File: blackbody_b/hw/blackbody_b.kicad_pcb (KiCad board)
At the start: 4 copper layers, 90 x 60 mm, 53 parts, among them IC101 TSL25911FN, IC201 ADM3055EBRIZ, J101 43650-0227, J201 43650-0427, J202 43650-0427, U101 NUCLEO-L432KC

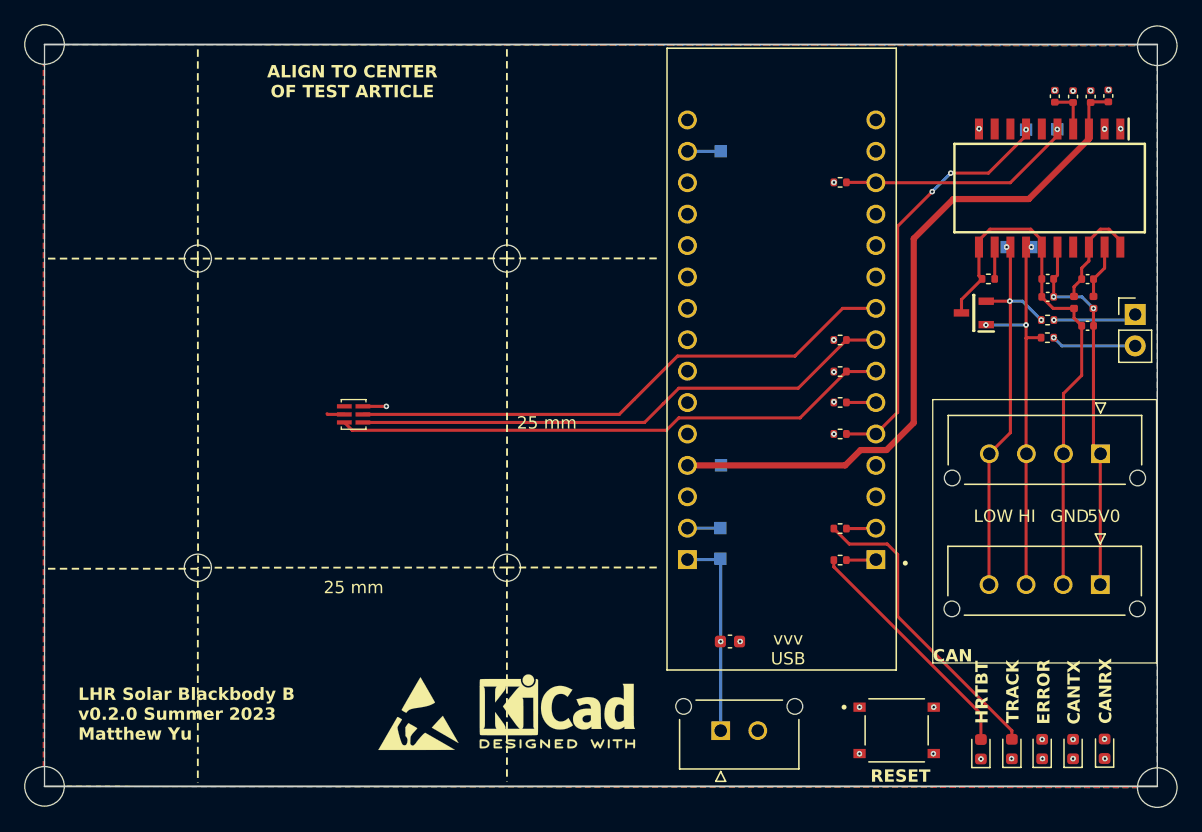
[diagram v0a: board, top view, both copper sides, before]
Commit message: fixes for blackbody b before prod
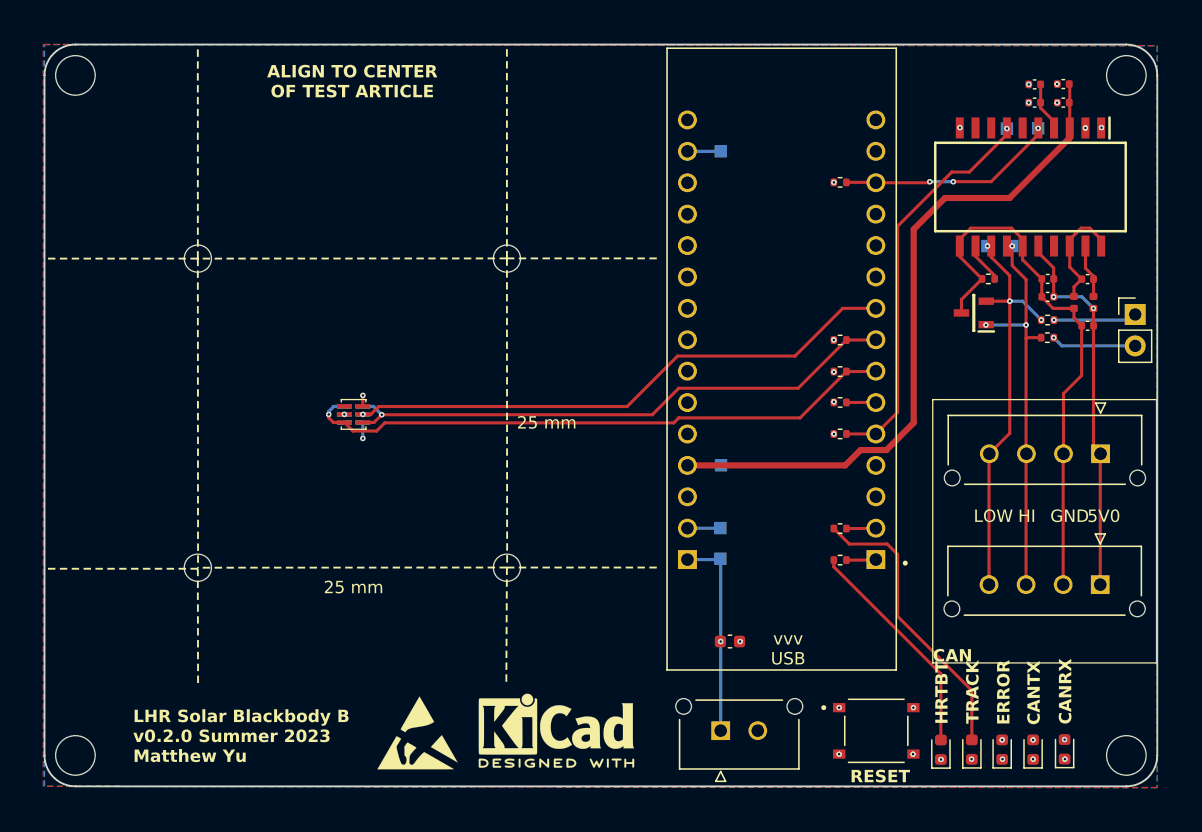
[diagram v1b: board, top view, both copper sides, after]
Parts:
- added IC102: TSL25911FN, footprints:ams_TSL25911FN, B.Cu at (115.0, 89.9)
- moved C201 3.76 mm to (172.4, 63.2), turned to 180 degrees
- moved H102 3.61 mm to (177.5, 117.5)
- moved H103 3.54 mm to (92.5, 62.5)
- moved H104 3.54 mm to (92.5, 117.5)
- moved H101 3.47 mm to (177.5, 62.5)
- moved D102 3.24 mm to (165.0, 117.0)
- moved D103 3.24 mm to (162.5, 117.0)
- moved D105 3.24 mm to (172.5, 117.0)
- moved D101 3.24 mm to (167.5, 117.0)
- moved D104 3.24 mm to (170.0, 117.0)
- moved C204 3.14 mm to (170.1, 64.7), turned to 180 degrees
- moved C202 2.27 mm to (172.4, 64.7), turned to 180 degrees
- moved C203 1.89 mm to (170.1, 63.2), turned to 180 degrees
- moved S101 1.65 mm to (157.3, 115.5)
- moved REF** 1.57 mm to (120.2, 115.7)
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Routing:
- net /SDA: track 45.2 -> 48.6 mm, vias 0 -> 1
- net Net-(D104-A): track 38.6 -> 35.6 mm
- net Net-(D105-A): track 57.9 -> 55.1 mm
- net /SCL: track 44.3 -> 46.1 mm, vias 0 -> 1
- net /CAN_RX: track 19.2 -> 17.7 mm, vias 1 -> 3
- net /CAN_TX: track 33.9 -> 32.3 mm, vias 3 -> 1
- net Net-(D201-K3): track 43.3 -> 44.7 mm
- net Net-(D102-A): track 24.8 -> 23.5 mm
- net Net-(D101-A): track 35.8 -> 34.5 mm
- net Net-(D103-A): track 19.4 -> 18.1 mm
- net +5V: track 59.3 -> 58.1 mm
- net +3V3: track 7.79 -> 6.77 mm, vias 2 -> 3
- net /comm_can/CAN_L: track 33.4 -> 34.2 mm
- net Net-(IC201-RS): track 2.57 -> 3.30 mm
- net /Reset: track 39.5 -> 38.9 mm
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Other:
- outline, holes or cut-outs redrawn

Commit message: update labels w/ kibuzzard, regen outputs
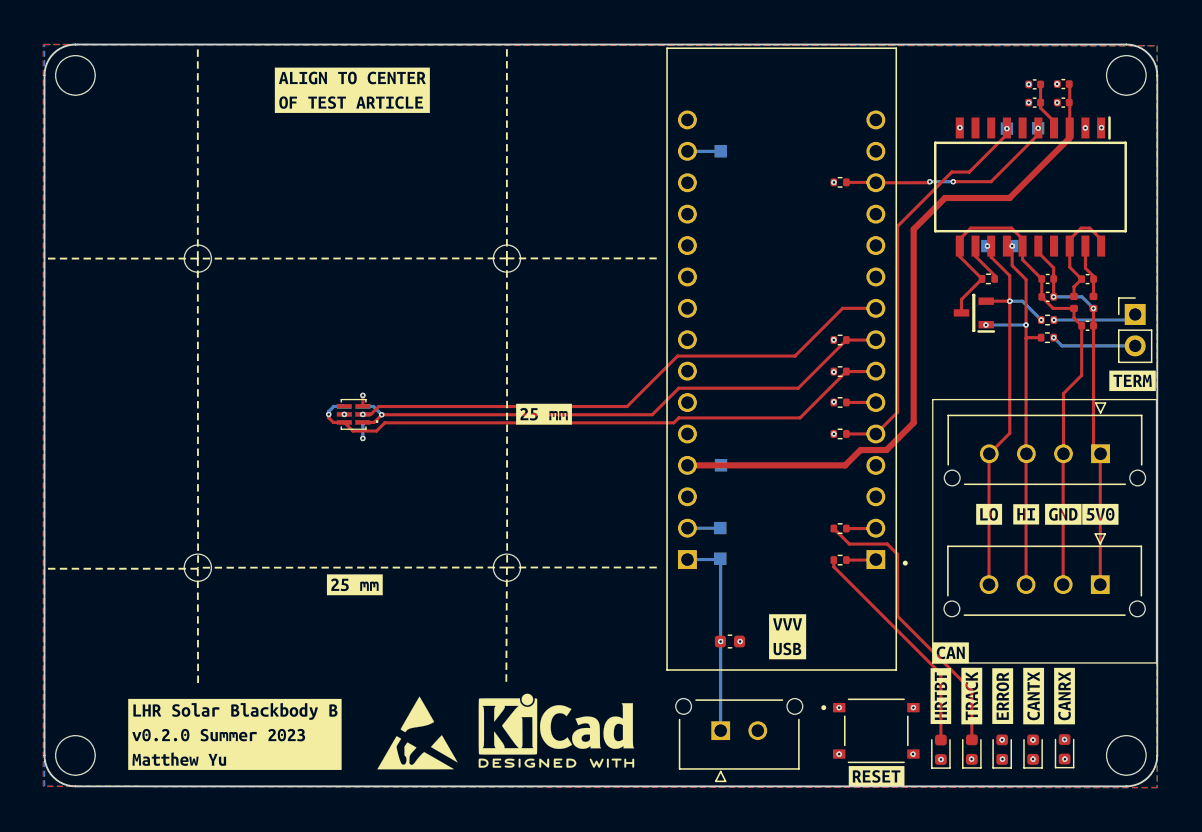
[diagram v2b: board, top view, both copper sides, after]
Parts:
- added kibuzzard-64E0E9DC: G***, kibuzzard-64E0E9DC, F.Cu at (157.3, 119.2)
- added kibuzzard-64E0E9E4: G***, kibuzzard-64E0E9E4, F.Cu at (162.5, 112.7)
- added kibuzzard-64E0E9FB: G***, kibuzzard-64E0E9FB, F.Cu at (165.0, 112.7)
- added kibuzzard-64E0EA02: G***, kibuzzard-64E0EA02, F.Cu at (167.5, 112.7)
- added kibuzzard-64E0EA0A: G***, kibuzzard-64E0EA0A, F.Cu at (170.0, 112.7)
- added kibuzzard-64E0EA10: G***, kibuzzard-64E0EA10, F.Cu at (172.5, 112.7)
- added kibuzzard-64E0EA63: G***, kibuzzard-64E0EA63, F.Cu at (163.3, 109.2)
- added kibuzzard-64E0EAD5: G***, kibuzzard-64E0EAD5, B.Cu at (147.3, 68.5)
- added kibuzzard-64E0EAF3: G***, kibuzzard-64E0EAF3, F.Cu at (169.4, 98.0)
- added kibuzzard-64E0EAF3: G***, kibuzzard-64E0EAF3, B.Cu at (168.5, 74.1)
- added kibuzzard-64E0EAFD: G***, kibuzzard-64E0EAFD, F.Cu at (172.4, 98.0)
- added kibuzzard-64E0EB06: G***, kibuzzard-64E0EB06, F.Cu at (175.4, 98.0)
- added kibuzzard-64E0EB26: G***, kibuzzard-64E0EB26, F.Cu at (178.0, 87.2)
- added kibuzzard-64E0EB3C: G***, kibuzzard-64E0EB3C, F.Cu at (150.1, 107.9)
- added kibuzzard-64E0EB48: G***, kibuzzard-64E0EB48, B.Cu at (147.2, 93.9)
- added kibuzzard-64E0EB4F: G***, kibuzzard-64E0EB4F, B.Cu at (147.2, 98.3)
- added kibuzzard-64E0EB63: G***, kibuzzard-64E0EB63, B.Cu at (147.2, 102.2)
- added kibuzzard-64E0EB95: G***, kibuzzard-64E0EB95, F.Cu at (166.4, 98.0)
- added kibuzzard-64E0EB95: G***, kibuzzard-64E0EB95, B.Cu at (166.0, 74.1)
- added kibuzzard-64E0EBC2: G***, kibuzzard-64E0EBC2, B.Cu at (167.6, 68.9)
- added kibuzzard-64E0EBCA: G***, kibuzzard-64E0EBCA, B.Cu at (170.7, 68.9)
- added kibuzzard-64E0F3D1: G***, kibuzzard-64E0F3D1, F.Cu at (114.9, 63.7)
- added kibuzzard-64E0F3E7: G***, kibuzzard-64E0F3E7, F.Cu at (105.4, 115.8)
- added kibuzzard-64E0F3F9: G***, kibuzzard-64E0F3F9, F.Cu at (130.4, 89.9)
- added kibuzzard-64E0F3F9: G***, kibuzzard-64E0F3F9, F.Cu at (115.1, 103.7)
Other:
- board text added: "."
- board text removed: "25 mm"
- board text removed: "3V3"
- board text removed: "5V"
- board text removed: "5V0"
- board text removed: "9V"
- board text removed: "ALIGN TO CENTER OF TEST ARTICLE"
- board text removed: "CAN"
- board text removed: "CANRX"
- board text removed: "CANTX"
- board text removed: "ERROR"
- board text removed: "GND"
- board text removed: "HI"
- board text removed: "HRTBT"
- board text removed: "LHR Solar Blackbody B v0.2.0 Summer 2023 Matthew Yu"
- board text removed: "LO"
- board text removed: "LOW"
- board text removed: "RESET"
- board text removed: "RX"
- board text removed: "TRACK"
- board text removed: "TX"
- board text removed: "vvv USB"
